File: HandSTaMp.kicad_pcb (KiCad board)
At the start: 2 copper layers, 40.6 x 16.5 mm, 24 parts, among them J1 USB_C_Receptacle_USB2.0_16P, J2 Pins, J3 SWD, SW0 BOOT, SW1 Row 0, Col 0, SW2 Row 0, Col 1, U1 STM32C071GBUx, U2 PRTR5V0U2X, U3 XC6206P332MR-G

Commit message: Minor tweaks
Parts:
- moved R4 0.19 mm to (149.2, 51.2)
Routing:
- net GND: track 15.0 -> 16.7 mm

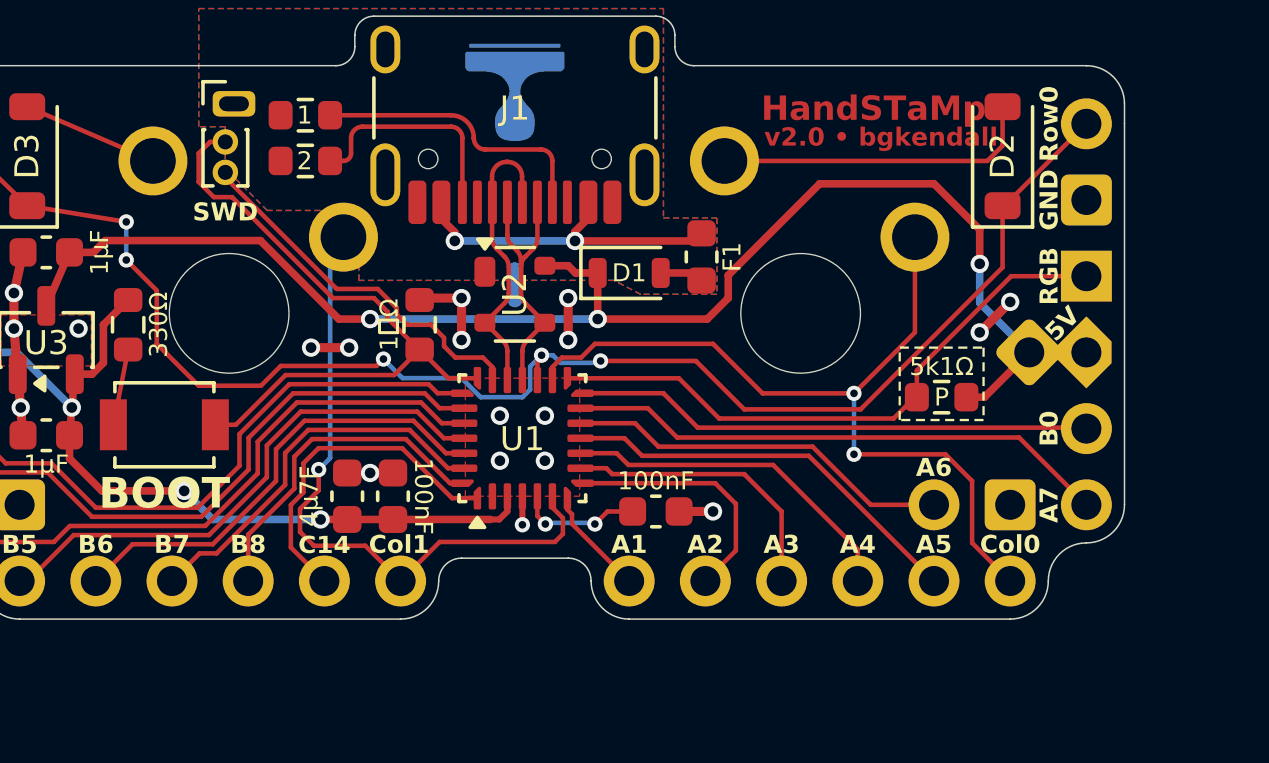
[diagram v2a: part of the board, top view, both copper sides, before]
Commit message: Move extra pin to short side
This better avoids the switch as the left and right sides taper in a bit compared to the top and bottom sides, which are more straight.
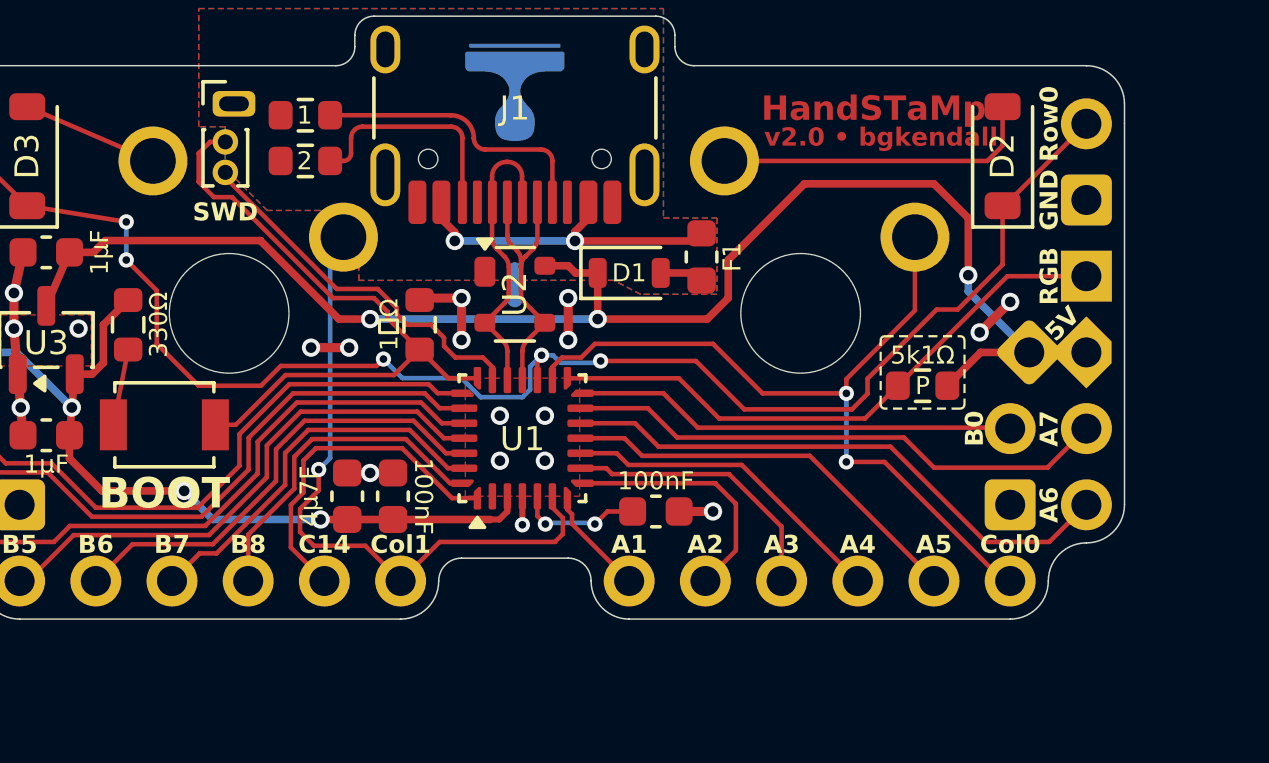
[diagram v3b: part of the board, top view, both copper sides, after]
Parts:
- moved R3 0.74 mm to (166.0, 53.2)
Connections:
- J2 pad 21: PA7 -> PB0
- J2 pad 22: PB0 -> PA7
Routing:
- net PA6: track 12.9 -> 19.0 mm
- net PB0: track 17.2 -> 14.7 mm
- net C0: track 27.7 -> 26.8 mm
- net VCC: track 47.4 -> 48.1 mm
- net PA4: track 11.6 -> 11.0 mm

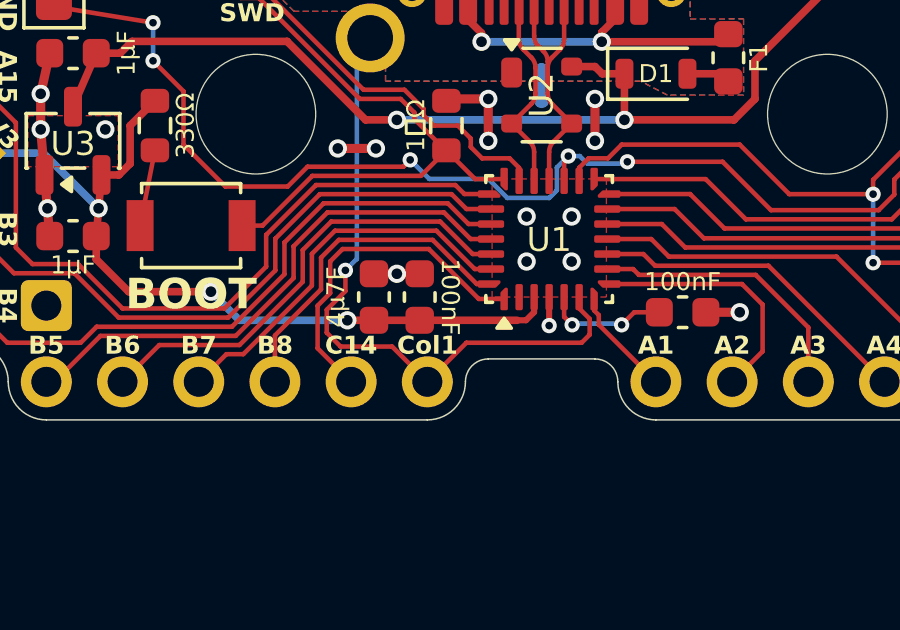
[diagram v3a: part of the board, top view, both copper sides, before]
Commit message: Add pad for PC15 access
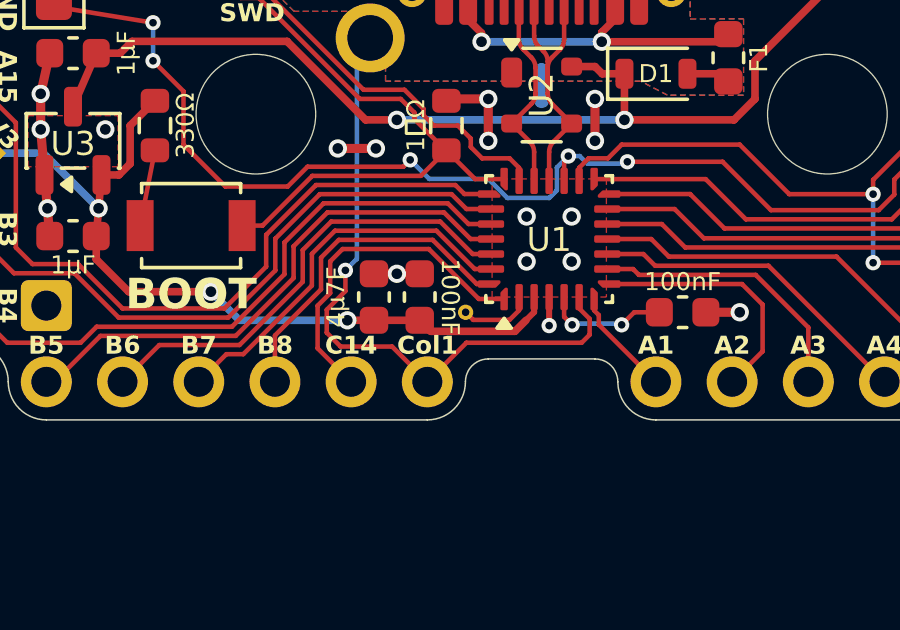
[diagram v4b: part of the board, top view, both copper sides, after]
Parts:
- added J4: C15, Project Library:TestPoint_Pad_1.5x1.5mm, B.Cu at (150.2, 57.0)
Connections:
- U1 pad 2: unconnected-(U1-PC15-Pad2) -> PC15
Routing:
- net PC15: track 0.00 -> 2.47 mm
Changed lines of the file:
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@@
 			(layers "F.Cu" "F.Mask" "F.Paste")
 			(roundrect_rratio 0.25)
-			(net "unconnected-(U1-PC15-Pad2)")
+			(net "PC15")
 			(pinfunction "PC15_2")
-			(pintype "bidirectional+no_connect")
+			(pintype "bidirectional")
 		)
 		(pad "3" smd roundrect
@@
 		)
 	)
+	(footprint "Project Library:TestPoint_Pad_1.5x1.5mm"
+		(layer "B.Cu")
+		(at 150.241 57.029 180)
+		(descr "SMD rectangular pad as test Point, square 1.5mm side length")
+		(tags "test point SMD pad rectangle square")
+		(property "Reference" "J4"
+			(at 0 1.648 0)
+			(layer "B.SilkS")
+			(hide yes)
+			(effects
+				(font
+					(size 1 1)
+					(thickness 0.15)
+				)
+				(justify mirror)
+			)
+		)
+		(property "Value" "C15"
+			(at -1.397 0 270)
+			(unlocked yes)
+			(layer "B.SilkS")
+			(effects
+				(font
+					(size 0.6 0.6)
+					(thickness 0.1)
+				)
+				(justify mirror)
+			)
+		)
+		(property "Datasheet" ""
+			(at 0 0 0)
+			(unlocked yes)
+			(layer "B.Fab")
+			(hide yes)
+			(effects
+				(font
+					(size 1.27 1.27)
+					(thickness 0.15)
+				)
+				(justify mirror)
+			)
+		)
+		(property "Description" ""
+			(at 0 0 0)
+			(unlocked yes)
+			(layer "B.Fab")
+			(hide yes)
+			(effects
+				(font
+					(size 1.27 1.27)
+					(thickness 0.15)
+				)
+				(justify mirror)
+			)
+		)
+		(property ki_fp_filters "Connector*:*_1x??_*")
+		(sheetname "/")
+		(sheetfile "HandSTaMp.kicad_sch")
+		(attr exclude_from_pos_files exclude_from_bom)
+		(duplicate_pad_numbers_are_jumpers no)
+		(fp_rect
+			(start -1 1)
+			(end 1 -1)
+			(stroke
+				(width 0.05)
+				(type solid)
+			)
+			(fill no)
+			(layer "B.CrtYd")
+		)
+		(fp_text user "${REFERENCE}"
+			(at 0 1.65 0)
+			(layer "B.Fab")
+			(effects
+				(font
+					(size 1 1)
+					(thickness 0.15)
+				)
+				(justify mirror)
+			)
+		)
+		(pad "1" thru_hole circle
+			(at 0.375 -0.375 180)
+			(size 0.508 0.508)
+			(drill 0.254
+				(offset 0 0)
+			)
+			(layers "*.Cu" "B.Mask")
+			(remove_unused_layers no)
+			(net "PC15")
+			(pinfunction "Pin_1_1")
+			(pintype "passive")
+			(padstack
+				(mode custom)
+				(layer "B.Cu"
+					(shape roundrect)
+					(size 1.5 1.5)
+					(offset -0.375 0.375)
+					(roundrect_rratio 0.15)
+					(thermal_bridge_angle 45)
+					(zone_connect -1)
+				)
+			)
+		)
+		(embedded_fonts no)
+	)
 	(footprint "Project Library:SW_MX_1u_PlateMount"
 		(locked yes)
@@
 	)
 	(segment
+		(start 148.704 58.039)
+		(end 151.511 58.039)
+		(width 0.254)
+		(layer "F.Cu")
+		(net "+3V3")
+	)
+	(segment
 		(start 138.684 52.451)
 		(end 138.3085 52.8265)
@@
 	)
 	(segment
+		(start 146.812 57.671)
+		(end 148.336 57.671)
+		(width 0.254)
+		(layer "F.Cu")
+		(net "+3V3")
+	)
+	(segment
 		(start 152.15 57.4)
 		(end 152.15 56.900195)
@@
 	)
 	(segment
-		(start 148.335998 57.671)
-		(end 151.5872 57.671)
-		(width 0.254)
-		(layer "F.Cu")
-		(net "+3V3")
-	)
-	(segment
-		(start 148.335998 57.671)
-		(end 146.812 57.671)
+		(start 148.336 57.671)
+		(end 148.704 58.039)
 		(width 0.254)
 		(layer "F.Cu")
@@
 	)
 	(segment
-		(start 151.5872 57.671)
-		(end 151.879 57.671)
-		(width 0.2032)
+		(start 145.923 57.671)
+		(end 146.812 57.671)
+		(width 0.254)
 		(layer "F.Cu")
 		(net "+3V3")
 	)
 	(segment
-		(start 145.923 57.671)
-		(end 146.812 57.671)
+		(start 151.511 58.039)
+		(end 151.879 57.671)
 		(width 0.254)
 		(layer "F.Cu")
@@
 	)
 	(segment
+		(start 153.65 57.273227)
+		(end 154.0002 57.623427)
+		(width 0.1524)
+		(layer "F.Cu")
+		(net "C1")
+	)
+	(segment
+		(start 149.8917 58.42)
+		(end 148.59 59.7217)
+		(width 0.1524)
+		(layer "F.Cu")
+		(net "C1")
+	)
+	(segment
 		(start 145.2372 57.320168)
 		(end 145.2372 58.0843)
@@
 	)
 	(segment
-		(start 153.65 57.273227)
-		(end 154.0002 57.623427)
+		(start 154.0002 58.1533)
+		(end 153.7335 58.42)
 		(width 0.1524)
 		(layer "F.Cu")
@@
 	)
 	(segment
-		(start 154.0002 58.1533)
-		(end 153.7335 58.42)
-		(width 0.1524)
-		(layer "F.Cu")
-		(net "C1")
-	)
-	(segment
-		(start 149.8917 58.42)
-		(end 148.59 59.7217)
-		(width 0.1524)
-		(layer "F.Cu")
-		(net "C1")
-	)
-	(segment
 		(start 145.8595 56.007)
 		(end 145.8595 56.697868)
@@
 		(net "Net-(D2-A)")
 	)
+	(segment
+		(start 151.65 57.337694)
+		(end 151.65 56.900195)
+		(width 0.1524)
+		(layer "F.Cu")
+		(net "PC15")
+	)
+	(segment
+		(start 151.329694 57.658)
+		(end 151.65 57.337694)
+		(width 0.1524)
+		(layer "F.Cu")
+		(net "PC15")
+	)
+	(segment
+		(start 150.12 57.658)
+		(end 151.329694 57.658)
+		(width 0.1524)
+		(layer "F.Cu")
+		(net "PC15")
+	)
+	(segment
+		(start 149.86 57.404)
+		(end 149.866 57.404)
+		(width 0.1524)
+		(layer "F.Cu")
+		(net "PC15")
+	)
+	(segment
+		(start 149.866 57.404)
+		(end 150.12 57.658)
+		(width 0.1524)
+		(layer "F.Cu")
+		(net "PC15")
+	)
 	(zone

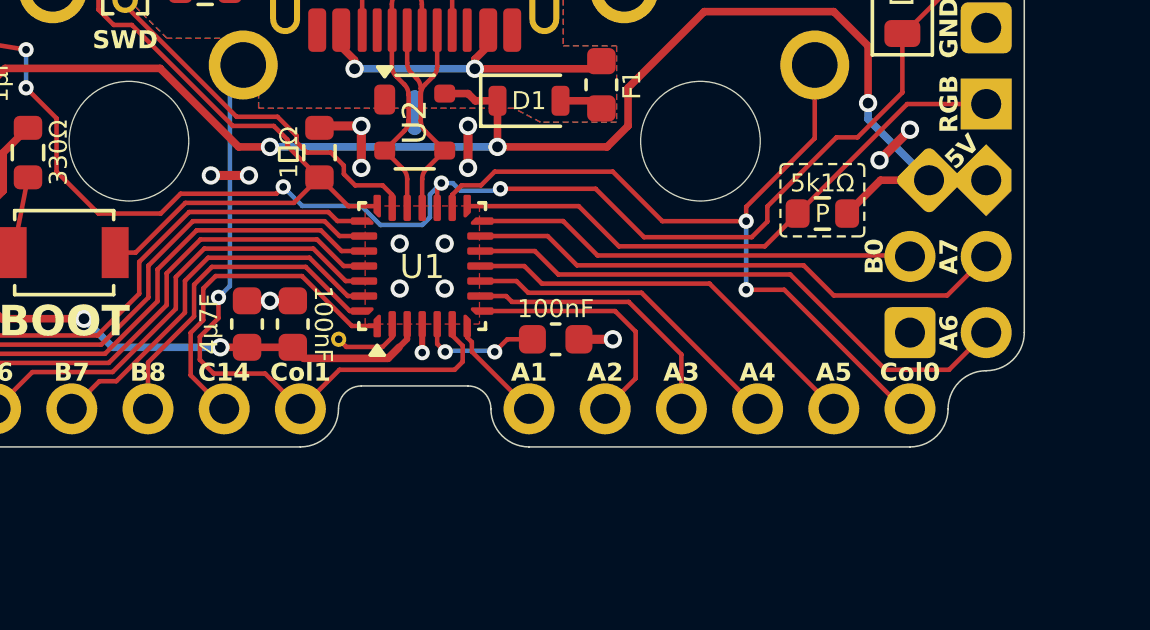
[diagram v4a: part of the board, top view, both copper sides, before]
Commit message: Move pad GPIO to THT connection
 * PC15 pad removed
 * Col1 switched to PC15
 * GND pin near right corner switched to GPIO
 * Bottom right pin assignments shuffled over one
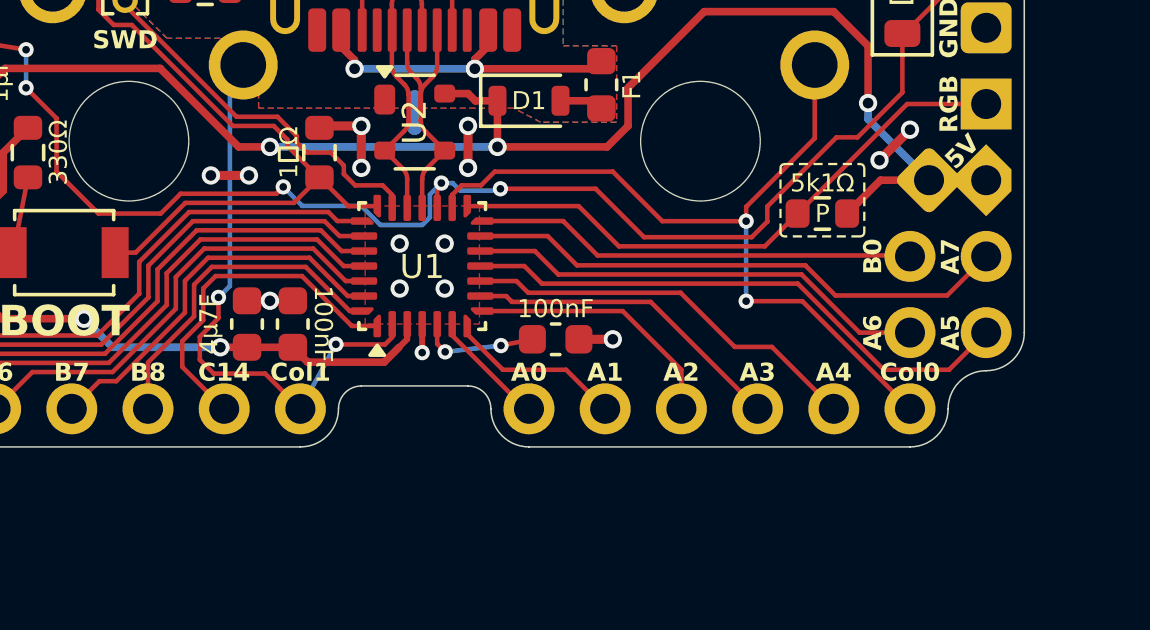
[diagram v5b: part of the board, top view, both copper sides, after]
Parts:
- removed J4: C15, Project Library:TestPoint_Pad_1.5x1.5mm
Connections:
- J2 pad 14: PA1 -> PA0
- J2 pad 15: PA2 -> PA1
- J2 pad 16: PA3 -> PA2
- J2 pad 17: PA4 -> PA3
- J2 pad 18: PA5 -> PA4
- J2 pad 21: PB0 -> PA5
- J2 pad 22: PA7 -> PB0
- J2 pad 23: RGB -> PA7
- U1 pad 2: PC15 -> C1
- U1 pad 6: C1 -> PA0
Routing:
- net PA5: track 13.8 -> 18.8 mm
- net PA0: track 0.00 -> 3.95 mm
- net PA6: track 19.0 -> 15.4 mm
- net PA4: track 11.0 -> 13.6 mm
- net C1: track 21.3 -> 18.8 mm, vias 1 -> 2
- net PC15: track 2.47 -> 0.00 mm
- net PA1: track 3.61 -> 5.90 mm
- net PA3: track 9.32 -> 10.8 mm

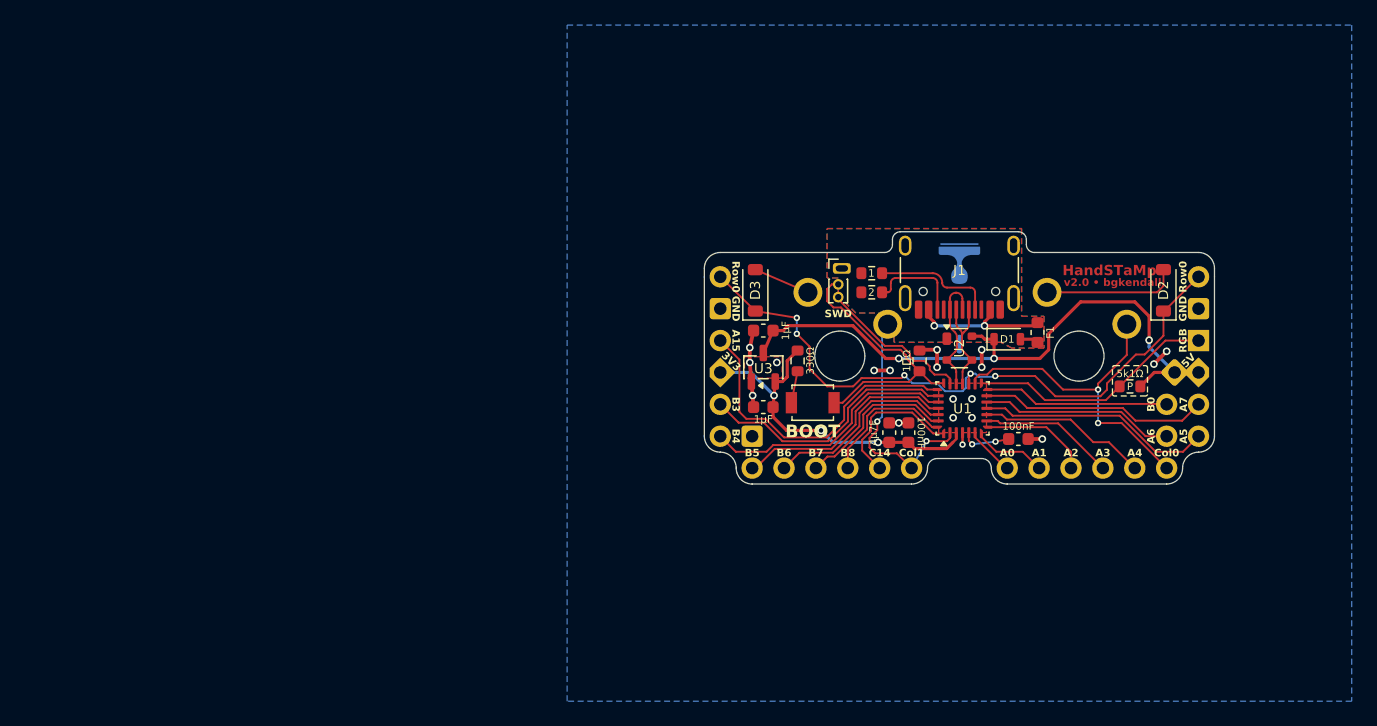
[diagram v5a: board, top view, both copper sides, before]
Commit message: Update schematic presentation, check ERC and DRC
Also, fix slight misalignment of external pins on PCB.
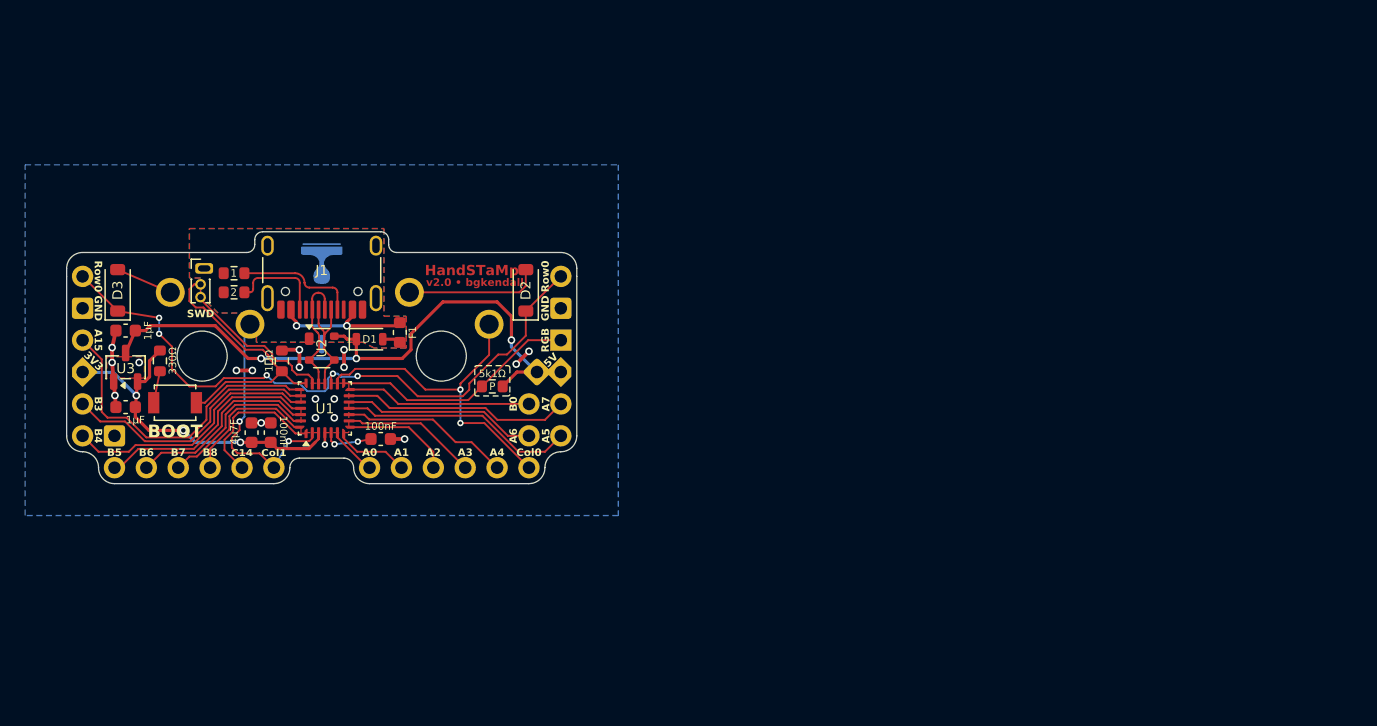
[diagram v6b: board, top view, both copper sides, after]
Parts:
- SW1: value Row 0, Col 0 -> Row 0, Col+0
- SW2: value Row 0, Col 1 -> Row 0, Col+1
- moved J3 50.8 mm to (101.6, 59.7)
- moved C3 50.8 mm to (96.0, 56.9)
- moved C4 50.8 mm to (97.5, 56.9)
- moved D1 50.8 mm to (105.4, 49.5)
- moved D2 50.8 mm to (117.9, 45.6)
- moved D3 50.8 mm to (85.3, 45.6)
- moved J1 50.8 mm to (101.6, 43.1)
- moved NT1 50.8 mm to (101.6, 49.8)
- moved R3 50.8 mm to (115.2, 53.2)
- moved SW0 50.8 mm to (89.9, 54.5)
- moved SW1 50.8 mm to (111.1, 50.8)
- moved U1 50.8 mm to (101.8, 55.0)
- moved U2 50.8 mm to (101.6, 50.2)
- moved C1 50.8 mm to (86.0, 48.8)
- moved C2 50.8 mm to (86.0, 54.9)
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- renumbered J3 to J2, J2 to J3
